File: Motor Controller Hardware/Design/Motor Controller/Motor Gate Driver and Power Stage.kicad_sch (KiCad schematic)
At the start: 25 parts, among them J25 Motor Power Connector, J8 Gate Driver EXT DRV_EN, U28 TSV911RILT

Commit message: A
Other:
- removed sheet Gate Driver U
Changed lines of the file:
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@@
-		)
-	)
-	(sheet
-		(at 311.277 -2.794)
-		(size 26.289 26.289)
-		(fields_autoplaced yes)
-		(stroke
-			(width 0.1524)
-			(type solid)
-		)
-		(fill
-			(color 0 0 0 0.0000)
-		)
-		(property "Sheetname" "Gate Driver U"
-			(at 311.277 -3.5056 0)
-			(effects
-				(font
-					(size 1.27 1.27)
-				)
-				(justify left bottom)
-			)
-		)
-		(property "Sheetfile" "gate_driver_u.kicad_sch"
-			(at 311.277 24.0796 0)
-			(effects
-				(font
-					(size 1.27 1.27)
-				)
-				(justify left top)
-			)
-		)
-		(pin "LOFF" input
-			(at 337.566 15.24 0)
-			(effects
-				(font
-					(size 1.27 1.27)
-				)
-				(justify right)
-			)
-		)
-		(pin "LON" input
-			(at 337.566 12.7 0)
-			(effects
-				(font
-					(size 1.27 1.27)
-				)
-				(justify right)
-			)
-		)
-		(pin "HOFF" input
-			(at 337.566 7.62 0)
-			(effects
-				(font
-					(size 1.27 1.27)
-				)
-				(justify right)
-			)
-		)
-		(pin "HON" input
-			(at 337.566 5.08 0)
-			(effects
-				(font
-					(size 1.27 1.27)
-				)
-				(justify right)
-			)
-		)
-		(pin "SW" input
-			(at 337.566 10.16 0)
-			(effects
-				(font
-					(size 1.27 1.27)
-				)
-				(justify right)
-			)
-		)
-		(pin "~{SD}{slash}OD" input
-			(at 311.277 17.78 180)
-			(effects
-				(font
-					(size 1.27 1.27)
-				)
-				(justify left)
-			)
-		)
-		(pin "PWM_L" input
-			(at 311.277 15.24 180)
-			(effects
-				(font
-					(size 1.27 1.27)
-				)
-				(justify left)
-			)
-		)
-		(pin "PWM_H" input
-			(at 311.277 12.7 180)
-			(effects
-				(font
-					(size 1.27 1.27)
-				)
-				(justify left)
-			)
-		)
-		(instances
-			(project "Motor Controller"
-				(path "/480a1464-7c70-42e1-b2f7-69e659e11383/c39e9a42-301a-4d13-bc72-bf7c010c94d6"
-					(page "19")
-				)
-			)
 		)
 	)

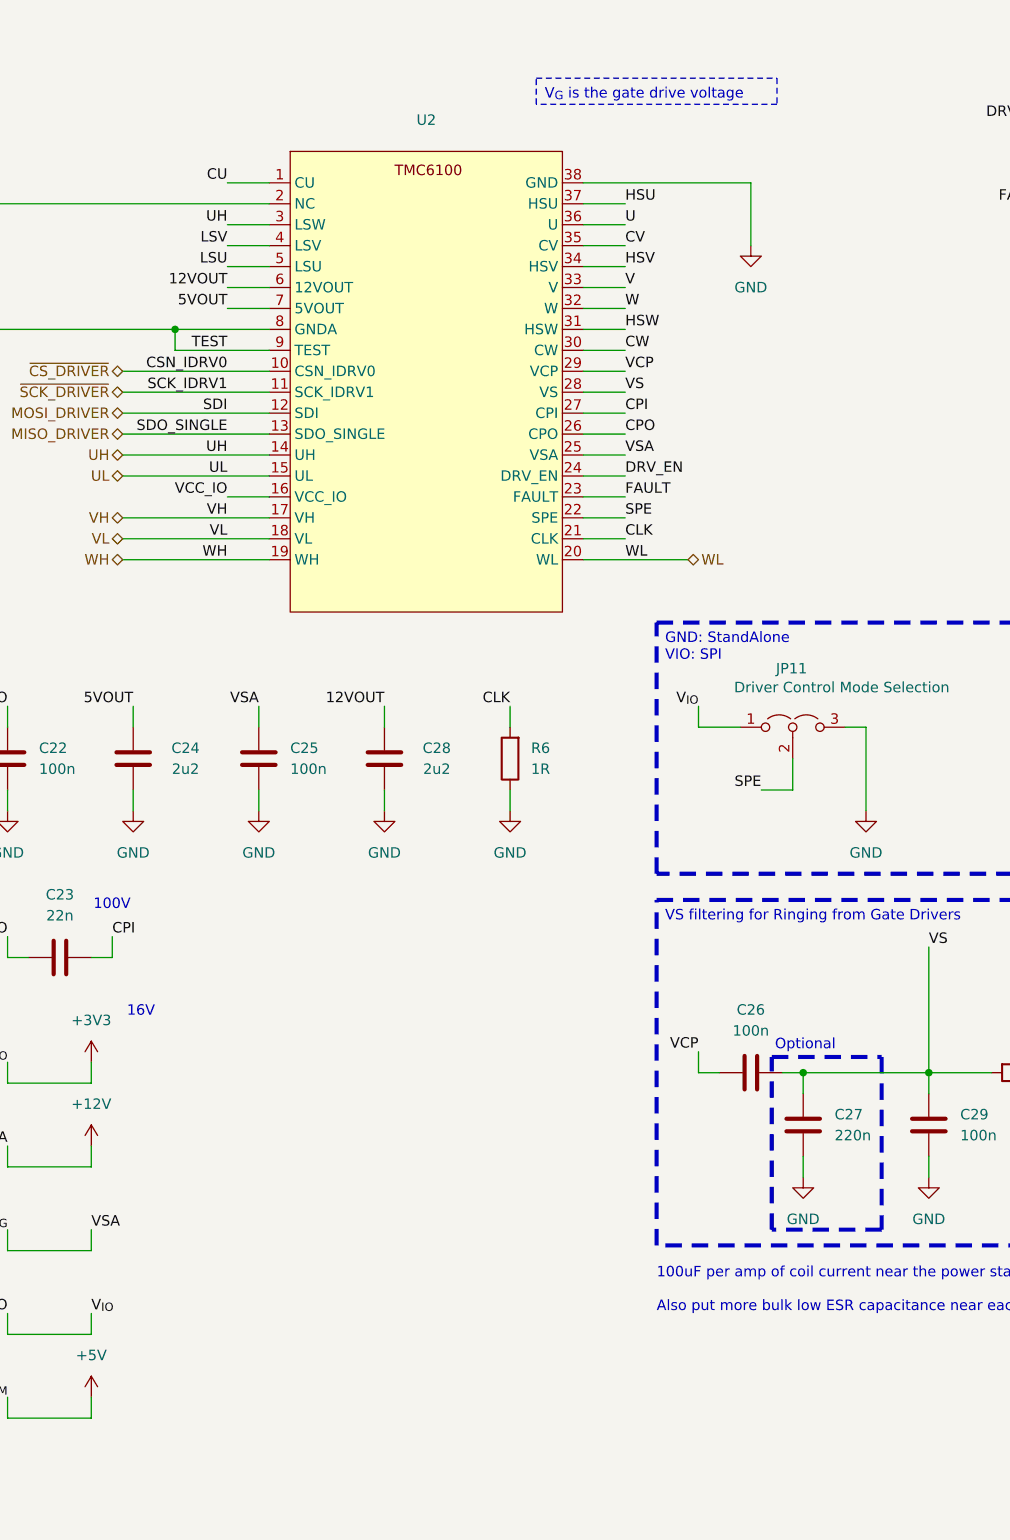
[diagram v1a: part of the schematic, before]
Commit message: Arranged most footprints will route soon
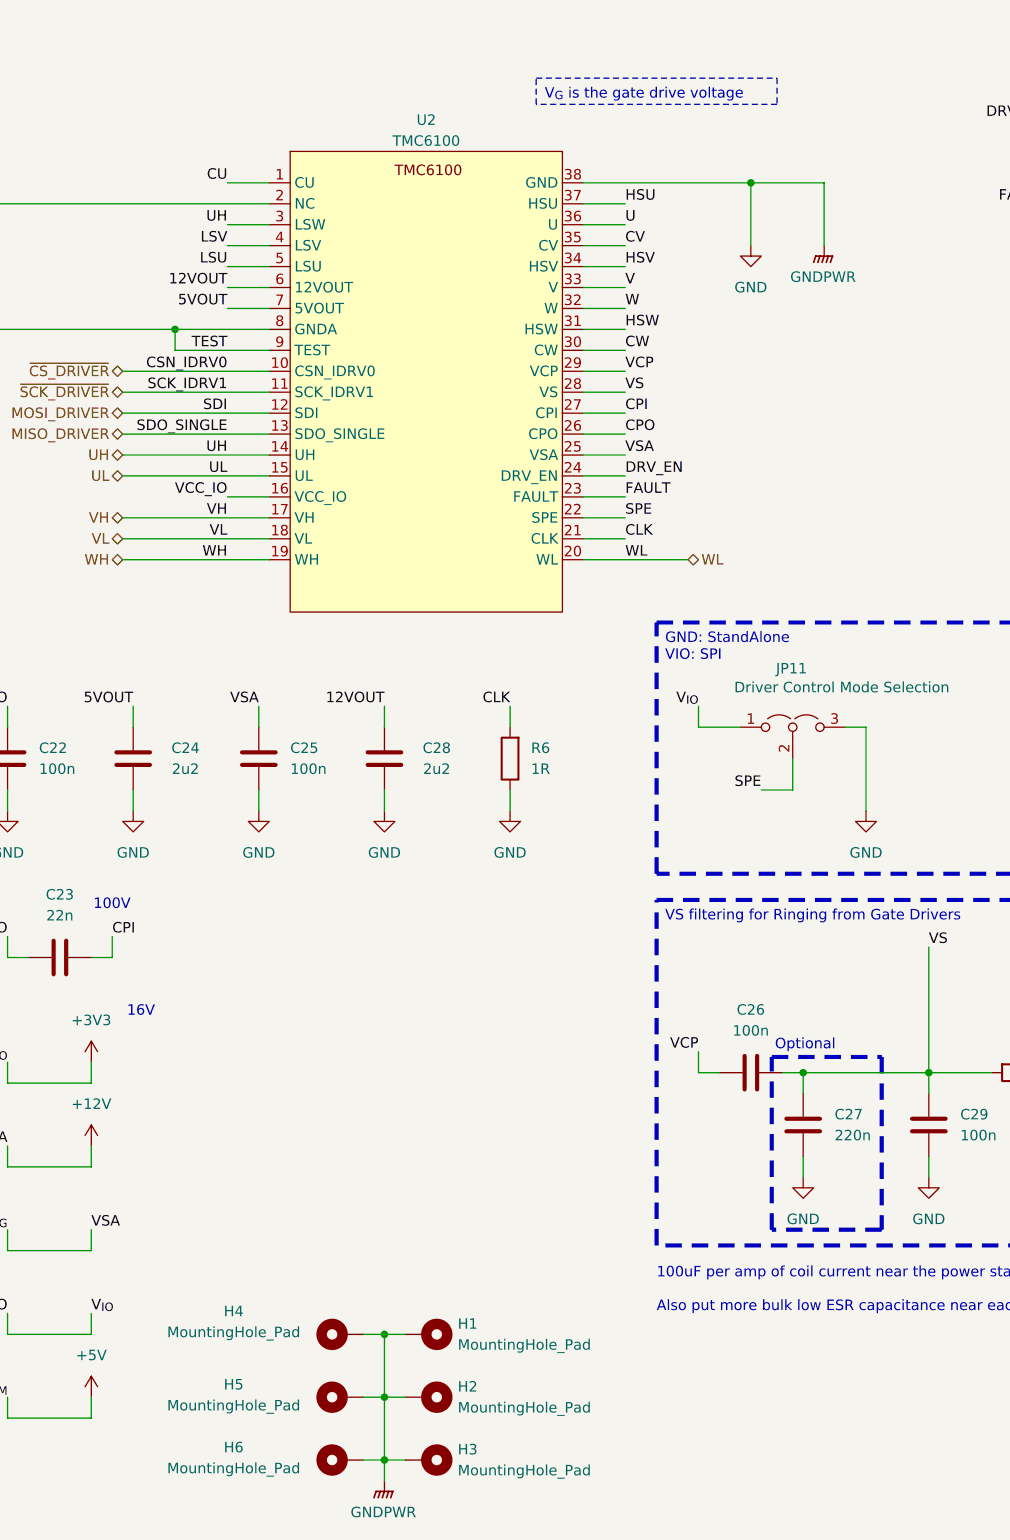
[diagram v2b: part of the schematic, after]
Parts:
- added H1, H2, H3, H4, H5, H6: MountingHole_Pad, symbol Mechanical:MountingHole_Pad
- U2: value ~ -> TMC6100; LCSC Part# (none) -> C3655384
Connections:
- net GNDPWR is gone; now on net GND: J25.1 (Pin_1)
- net GND: now also H1.1, H2.1, H3.1, H4.1, H5.1, H6.1

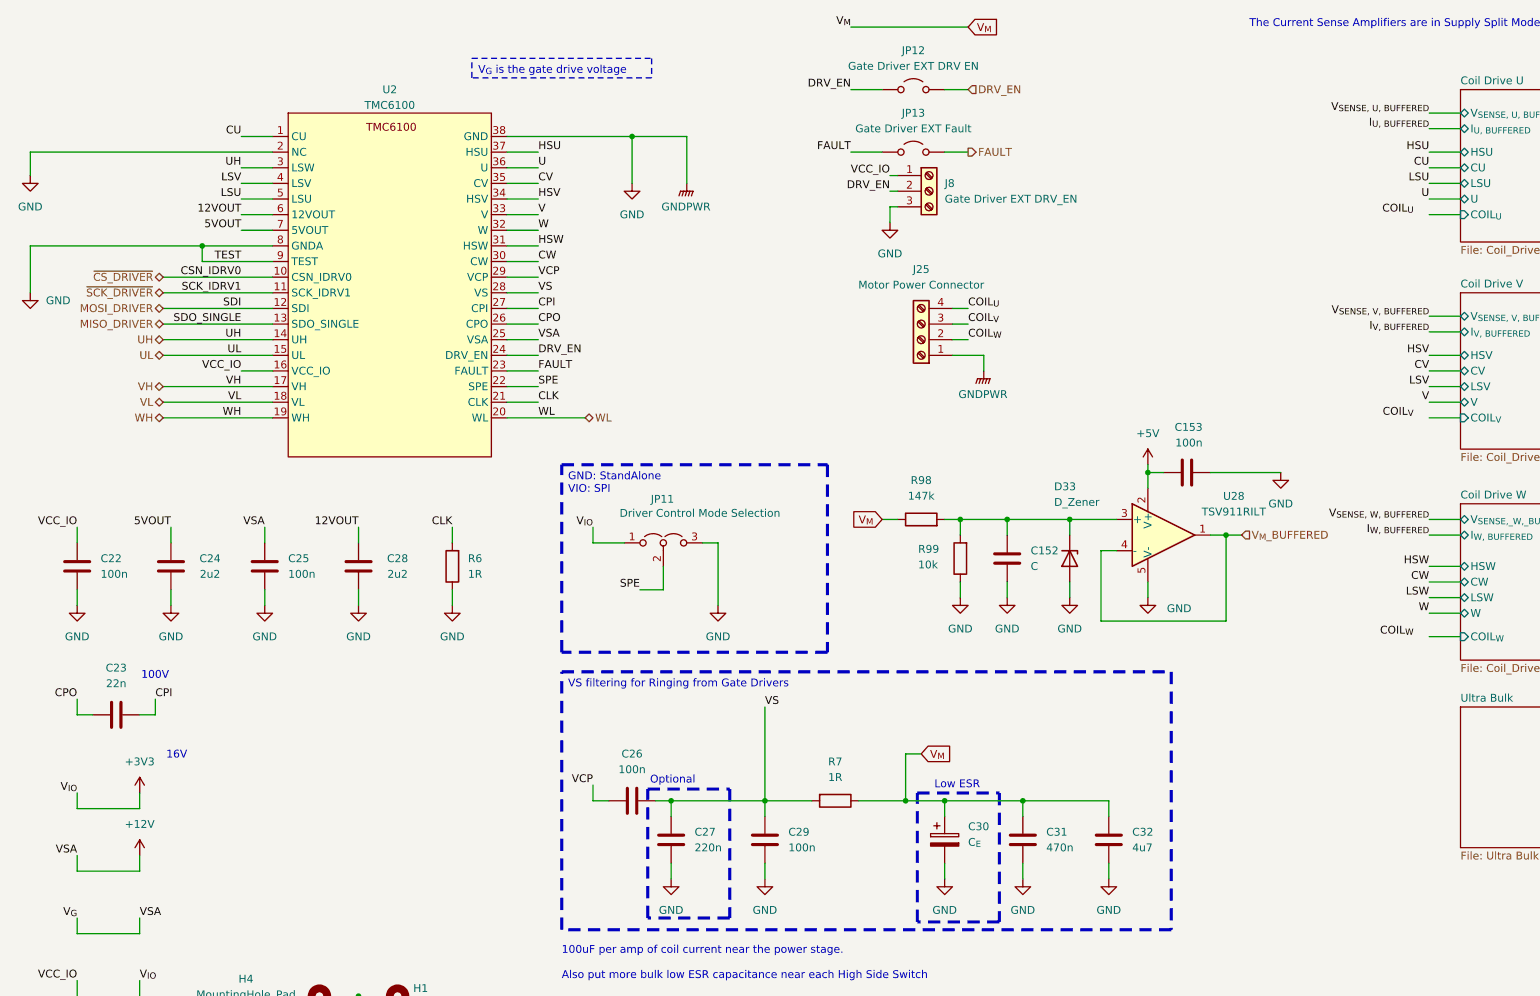
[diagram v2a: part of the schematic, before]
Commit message: made some layout changes and started routing power stage
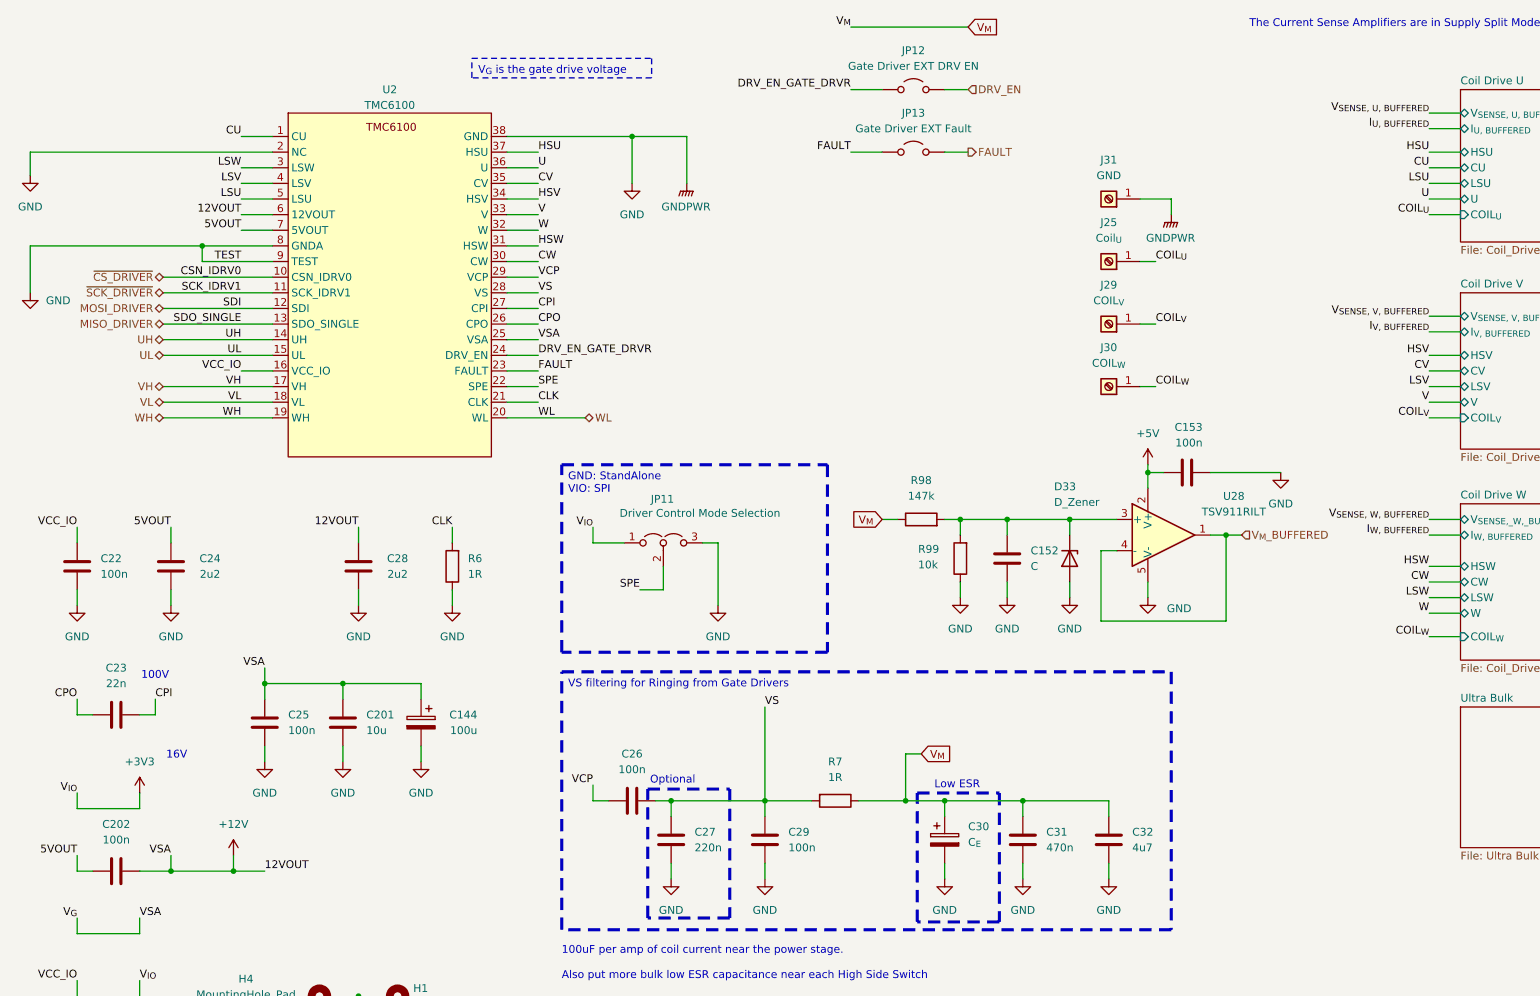
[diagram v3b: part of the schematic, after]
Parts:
- removed J25: Motor Power Connector, TerminalBlock_Phoenix:TerminalBlock_Phoenix_MKDS-1,5-4_1x04_P5.00mm_Horizontal, symbol Connector:Screw_Terminal_01x04
- removed J8: Gate Driver EXT DRV_EN, TerminalBlock_Phoenix:TerminalBlock_Phoenix_MPT-0,5-3-2.54_1x03_P2.54mm_Horizontal, symbol Connector:Screw_Terminal_01x03
- added C144: 100u, Capacitor_SMD:CP_Elec_6.3x9.9, symbol Device:C_Polarized
- added C201: 10u, Capacitor_SMD:C_1210_3225Metric, symbol Device:C
- added C202: 100n, Capacitor_SMD:C_0603_1608Metric, symbol Device:C
- added J25: Coil_{U}, ecocad:KEYSTONE_7691, symbol Connector:Screw_Terminal_01x01
- added J29: COIL_{V}, ecocad:KEYSTONE_7691, symbol Connector:Screw_Terminal_01x01
- added J30: COIL_{W}, ecocad:KEYSTONE_7691, symbol Connector:Screw_Terminal_01x01
- added J31: GND, ecocad:KEYSTONE_7691, symbol Connector:Screw_Terminal_01x01
- JP11: footprint Connector_PinHeader_2.54mm:PinHeader_1x03_P2.54mm_Vertical -> Connector_PinHeader_1.27mm:PinHeader_1x03_P1.27mm_Vertical
- JP12, JP13: footprint Connector_PinHeader_2.54mm:PinHeader_1x02_P2.54mm_Vertical -> Connector_PinHeader_1.27mm:PinHeader_1x02_P1.27mm_Vertical
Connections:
- net 12VOUT is gone; now on net +12V: C28.1, U2.6 (12VOUT)
- net +12V: now also C144.1, C201.1, C202.2
- net 5VOUT: now also C202.1
- net COIL_{U}: now also J25.1 (Pin_1)
- net COIL_{V}: now also J29.1 (Pin_1)
- net COIL_{W}: now also J30.1 (Pin_1)
- net DRV_EN: no longer JP12.1 (A), U2.24 (DRV_EN)
- net GND: now also C144.2, C201.2, J31.1 (Pin_1)
- net LSW: now also U2.3 (LSW)
- net UH: no longer U2.3 (LSW)
- new net DRV_EN_GATE_DRVR: JP12.1 (A), U2.24 (DRV_EN)
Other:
- moved on the sheet: C25

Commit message: A
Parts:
- J25, J29, J30, J31: footprint ecocad:KEYSTONE_7691 -> ecocad_lib_footprints:KEYSTONE_7691
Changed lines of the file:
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@@
 			)
 		)
-		(property "Footprint" "ecocad:KEYSTONE_7691"
+		(property "Footprint" "ecocad_lib_footprints:KEYSTONE_7691"
 			(at 193.04 63.5 0)
 			(effects
@@
 			)
 		)
-		(property "Footprint" "ecocad:KEYSTONE_7691"
+		(property "Footprint" "ecocad_lib_footprints:KEYSTONE_7691"
 			(at 193.04 43.18 0)
 			(effects
@@
 			)
 		)
-		(property "Footprint" "ecocad:KEYSTONE_7691"
+		(property "Footprint" "ecocad_lib_footprints:KEYSTONE_7691"
 			(at 193.04 53.34 0)
 			(effects
@@
 			)
 		)
-		(property "Footprint" "ecocad:KEYSTONE_7691"
+		(property "Footprint" "ecocad_lib_footprints:KEYSTONE_7691"
 			(at 193.04 73.66 0)
 			(effects

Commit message: A
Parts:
- added NT2: PGND TIE, NetTie:NetTie-2_SMD_Pad0.5mm, symbol Device:NetTie_2
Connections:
- net GND: now also NT2.1, NT2.2

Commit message: Updated 3d models
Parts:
- U2: footprint ecocad:QFN37_7X7_ADI -> ecocad_lib_footprints:QFN37_7X7_ADI
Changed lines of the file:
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@@
 			)
 		)
-		(property "Footprint" "ecocad:QFN37_7X7_ADI"
+		(property "Footprint" "ecocad_lib_footprints:QFN37_7X7_ADI"
 			(at 76.454 87.884 0)
 			(effects

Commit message: AA
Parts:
- U2: DK# (none) -> 175-TMC6100-LA-TCT-ND
- U28: DK# (none) -> 497-10538-1-ND; LCSC Part# (none) -> C672321; LCSC# (none) -> C672321
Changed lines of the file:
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@@
 			)
 		)
-		(property "LCSC Part#" ""
+		(property "LCSC Part#" "C672321"
+			(at 201.93 97.79 0)
+			(effects
+				(font
+					(size 1.27 1.27)
+				)
+				(hide yes)
+			)
+		)
+		(property "DK#" "497-10538-1-ND"
+			(at 201.93 97.79 0)
+			(effects
+				(font
+					(size 1.27 1.27)
+				)
+				(hide yes)
+			)
+		)
+		(property "LCSC#" "C672321"
 			(at 201.93 97.79 0)
 			(effects
@@
 			(at 76.2 45.72 0)
 			(effects
+				(font
+					(size 1.27 1.27)
+				)
+				(hide yes)
+			)
+		)
+		(property "DK#" "175-TMC6100-LA-TCT-ND"
+			(at 76.2 45.72 0)
+			(effects

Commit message: A
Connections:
- net DRV_EN renamed GATE_DRIVER_EXT_EN_IN
- net FAULT renamed FAULT_OUT
- net FAULT_OUT: no longer JP13.2 (B)
- new net GATE_DRIVER_FAULT_OUT: JP13.2 (B)
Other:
- moved on the sheet: JP12, JP13
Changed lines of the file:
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@@
 	(wire
 		(pts
-			(xy 151.13 25.4) (xy 156.21 25.4)
+			(xy 142.24 26.67) (xy 147.32 26.67)
 		)
 		(stroke
@@
 	(wire
 		(pts
-			(xy 151.13 15.24) (xy 170.18 15.24)
+			(xy 142.24 16.51) (xy 161.29 16.51)
 		)
 		(stroke
@@
 	(wire
 		(pts
-			(xy 166.37 25.4) (xy 170.18 25.4)
+			(xy 157.48 26.67) (xy 161.29 26.67)
 		)
 		(stroke
@@
 	(wire
 		(pts
-			(xy 166.37 35.56) (xy 170.18 35.56)
+			(xy 157.48 38.1) (xy 161.29 38.1)
 		)
 		(stroke
@@
 	(wire
 		(pts
-			(xy 151.13 35.56) (xy 156.21 35.56)
+			(xy 142.24 38.1) (xy 147.32 38.1)
 		)
 		(stroke
@@
 	)
 	(label "V_{M}"
-		(at 151.13 15.24 180)
+		(at 142.24 16.51 180)
 		(fields_autoplaced yes)
 		(effects
@@
 		)
 	)
-	(label "FAULT"
-		(at 151.13 35.56 180)
+	(label "FAULT_OUT"
+		(at 142.24 38.1 180)
 		(fields_autoplaced yes)
 		(effects
@@
 		)
 	)
-	(label "FAULT"
+	(label "FAULT_OUT"
 		(at 100.33 71.12 0)
 		(fields_autoplaced yes)
@@
 	)
 	(label "DRV_EN_GATE_DRVR"
-		(at 151.13 25.4 180)
+		(at 142.24 26.67 180)
 		(fields_autoplaced yes)
 		(effects
@@
 	(global_label "V_{M}"
 		(shape input)
-		(at 170.18 15.24 0)
+		(at 161.29 16.51 0)
 		(fields_autoplaced yes)
 		(effects
@@
 		)
 		(property "Intersheetrefs" "${INTERSHEET_REFS}"
-			(at 175.4657 15.24 0)
+			(at 166.5757 16.51 0)
 			(effects
 				(font
@@
 		)
 	)
-	(hierarchical_label "FAULT"
+	(hierarchical_label "GATE_DRIVER_FAULT_OUT"
 		(shape output)
-		(at 170.18 35.56 0)
+		(at 161.29 38.1 0)
 		(fields_autoplaced yes)
 		(effects
@@
 		)
 	)
-	(hierarchical_label "DRV_EN"
+	(hierarchical_label "GATE_DRIVER_EXT_EN_IN"
 		(shape input)
-		(at 170.18 25.4 0)
+		(at 161.29 26.67 0)
 		(fields_autoplaced yes)
 		(effects
@@
 	(symbol
 		(lib_id "Jumper:Jumper_2_Open")
-		(at 161.29 25.4 0)
+		(at 152.4 26.67 0)
 		(unit 1)
 		(exclude_from_sim yes)
@@
 		(fields_autoplaced yes)
 		(property "Reference" "JP12"
-			(at 161.29 19.05 0)
+			(at 152.4 20.32 0)
 			(effects
 				(font
@@
 		)
 		(property "Value" "Gate Driver EXT DRV EN"
-			(at 161.29 21.59 0)
+			(at 152.4 22.86 0)
 			(effects
 				(font
@@
 		)
 		(property "Footprint" "Connector_PinHeader_1.27mm:PinHeader_1x02_P1.27mm_Vertical"
-			(at 161.29 25.4 0)
+			(at 152.4 26.67 0)
 			(effects
 				(font
@@
 		)
 		(property "Datasheet" "~"
-			(at 161.29 25.4 0)
+			(at 152.4 26.67 0)
 			(effects
 				(font
@@
 		)
 		(property "Description" "Jumper, 2-pole, open"
-			(at 161.29 25.4 0)
+			(at 152.4 26.67 0)
 			(effects
 				(font
@@
 		)
 		(property "LCSC Part#" ""
-			(at 161.29 25.4 0)
+			(at 152.4 26.67 0)
 			(effects
 				(font
@@
 	(symbol
 		(lib_id "Jumper:Jumper_2_Open")
-		(at 161.29 35.56 0)
+		(at 152.4 38.1 0)
 		(unit 1)
 		(exclude_from_sim yes)
@@
 		(fields_autoplaced yes)
 		(property "Reference" "JP13"
-			(at 161.29 29.21 0)
+			(at 152.4 31.75 0)
 			(effects
 				(font
@@
 		)
 		(property "Value" "Gate Driver EXT Fault"
-			(at 161.29 31.75 0)
+			(at 152.4 34.29 0)
 			(effects
 				(font
@@
 		)
 		(property "Footprint" "Connector_PinHeader_1.27mm:PinHeader_1x02_P1.27mm_Vertical"
-			(at 161.29 35.56 0)
+			(at 152.4 38.1 0)
 			(effects
 				(font
@@
 		)
 		(property "Datasheet" "~"
-			(at 161.29 35.56 0)
+			(at 152.4 38.1 0)
 			(effects
 				(font
@@
 		)
 		(property "Description" "Jumper, 2-pole, open"
-			(at 161.29 35.56 0)
+			(at 152.4 38.1 0)
 			(effects
 				(font
@@
 		)
 		(property "LCSC Part#" ""
-			(at 161.29 35.56 0)
+			(at 152.4 38.1 0)
 			(effects
 				(font
